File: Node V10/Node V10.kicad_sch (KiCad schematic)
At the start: 6 parts, among them J1 Soil Sensor - 1, J2 Soil Sensor - 2, J3 Soil Sensor - 3, J4 Soil Sensor - 4, U1 MCU

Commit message: Completed schamtic
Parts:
- added J5: PiicoDev, symbol Connector_Generic:Conn_01x04
- added R1, R2: 10k, symbol Device:R
- added TP1: GND_Test, symbol Connector:TestPoint
- added TP2: Vbatt Test, symbol Connector:TestPoint
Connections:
- net SCL: now also J5.1 (Pin_1)
- net SDA: now also J5.2 (Pin_2)
- net GND: now reaches J1.2 (Pin_2)
- net GND: now also J2.2 (Pin_2), J3.2 (Pin_2), J4.2 (Pin_2), U1.100 (Vin_Batt), U1.8 (GND), U2.1 (OUT-), J5.4 (Pin_4), R2.2, TP1.1
- net +3V3: now reaches J1.3 (Pin_3)
- net +3V3: now also J2.3 (Pin_3), J3.3 (Pin_3), J4.3 (Pin_3), U1.9 (3V3), J5.3 (Pin_3)
- net +BATT: now reaches U2.2 (OUT+)
- net +BATT: now also U1.200 (GND_Batt), R1.1, TP2.1
- net Done: now reaches U2.3 (DNE)
- net Done: now also U1.12 (GP44)
- net Vbatt_sense: now reaches U1.5 (GP6)
- net Vbatt_sense: now also R1.2, R2.1
- no-connect marks 0 -> 5
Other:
- note added: "Sensors"
- company: (none) -> Liam Howell
- title: (none) -> PlantPulse Node
- moved on the sheet: J1, J2, J3, J4, U1B, U2

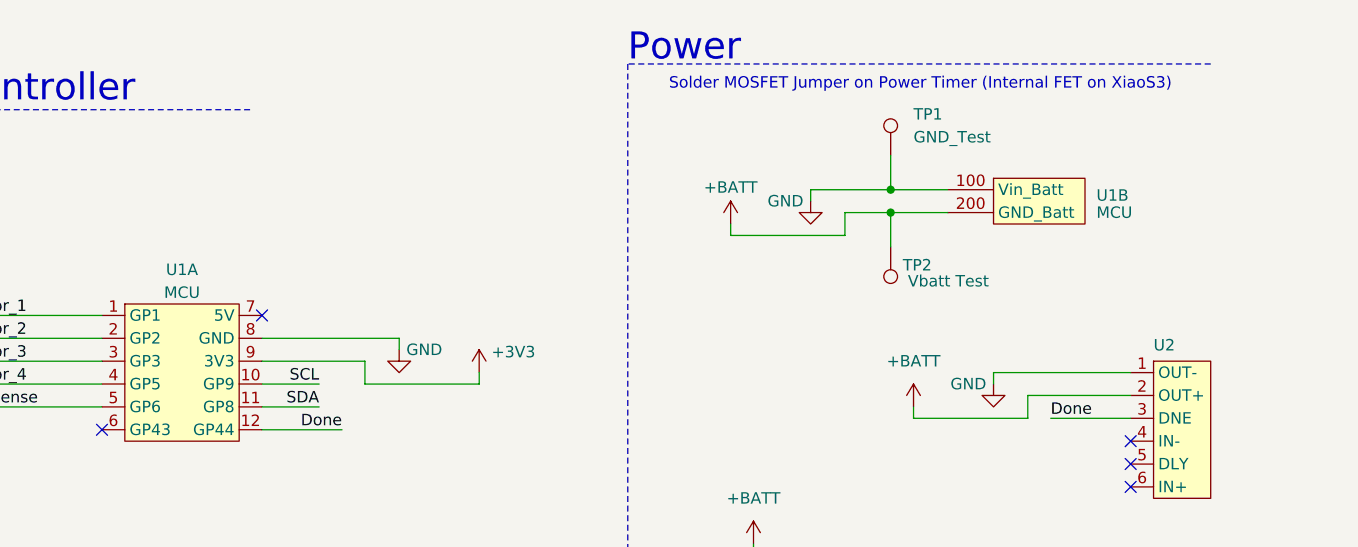
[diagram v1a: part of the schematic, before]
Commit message: Footprints assigned
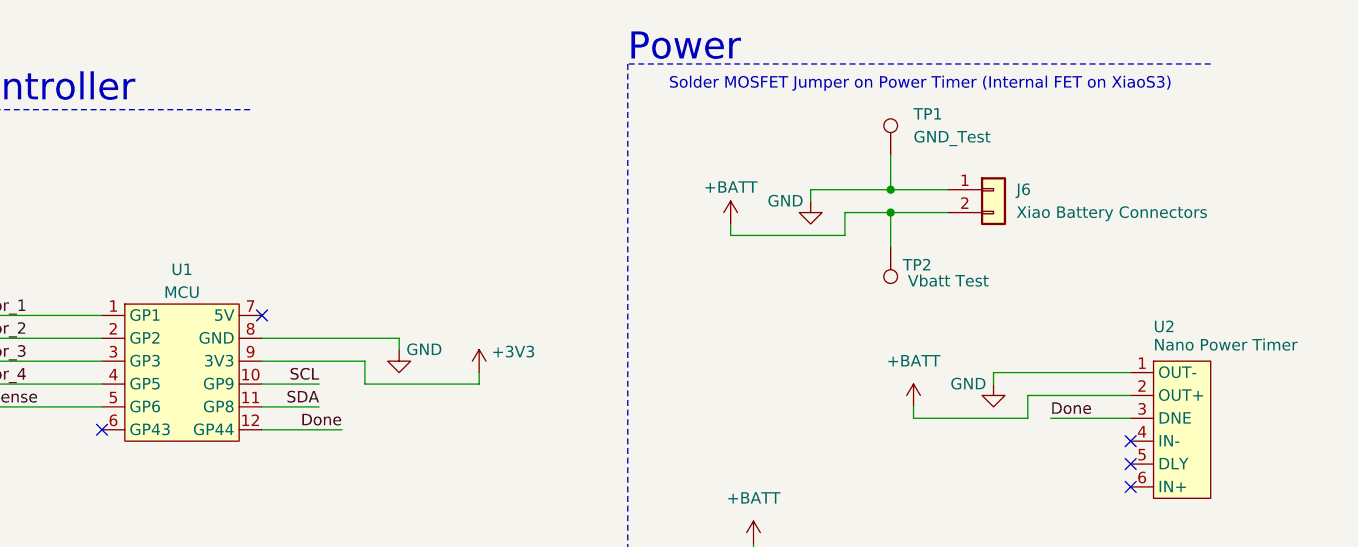
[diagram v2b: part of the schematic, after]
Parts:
- removed unit 2 of U1
- added J6: Xiao Battery Connectors, Connector_PinHeader_2.54mm:PinHeader_1x02_P2.54mm_Horizontal, symbol Connector_Generic:Conn_01x02
- J1, J2, J3, J4: footprint (none) -> Connector_PinHeader_2.54mm:PinHeader_1x03_P2.54mm_Vertical
- J5: footprint (none) -> Footprints-General:PiicoDev Breadboard
- R1, R2: footprint (none) -> Resistor_THT:R_Axial_DIN0207_L6.3mm_D2.5mm_P7.62mm_Horizontal
- TP1, TP2: footprint (none) -> TestPoint:TestPoint_THTPad_1.0x1.0mm_Drill0.5mm
- U1: footprint (none) -> Footprints-General:Xiao-S3
- U2: value ~ -> Nano Power Timer; footprint (none) -> Footprints-General:Nano Power Timer
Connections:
- net +BATT: now also J6.2 (Pin_2)
- net GND: now also J6.1 (Pin_1)
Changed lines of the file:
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@@
 			)
 		)
-		(property "Footprint" ""
+		(property "Footprint" "Connector_PinHeader_2.54mm:PinHeader_1x03_P2.54mm_Vertical"
 			(at 44.45 81.28 0)
 			(effects
@@
 					(reference "#PWR016")
 					(unit 1)
-				)
-			)
-		)
-	)
-	(symbol
-		(lib_id "Liam_Generic_symbols:Xiao_X3_w/_Batt")
-		(at 234.95 78.74 0)
-		(unit 2)
-		(exclude_from_sim no)
-		(in_bom yes)
-		(on_board yes)
-		(dnp no)
-		(fields_autoplaced yes)
-		(property "Reference" "U1"
-			(at 246.38 80.6449 0)
-			(effects
-				(font
-					(size 1.27 1.27)
-				)
-				(justify left)
-			)
-		)
-		(property "Value" "MCU"
-			(at 246.38 82.55 0)
-			(effects
-				(font
-					(size 1.27 1.27)
-				)
-				(justify left)
-			)
-		)
-		(property "Footprint" ""
-			(at 234.95 78.74 0)
-			(effects
-				(font
-					(size 1.27 1.27)
-				)
-				(hide yes)
-			)
-		)
-		(property "Datasheet" ""
-			(at 234.95 78.74 0)
-			(effects
-				(font
-					(size 1.27 1.27)
-				)
-				(hide yes)
-			)
-		)
-		(property "Description" ""
-			(at 234.95 78.74 0)
-			(effects
-				(font
-					(size 1.27 1.27)
-				)
-				(hide yes)
-			)
-		)
-		(pin "5"
-		)
-		(pin "9"
-		)
-		(pin "8"
-		)
-		(pin "3"
-		)
-		(pin "1"
-		)
-		(pin "11"
-		)
-		(pin "200"
-		)
-		(pin "4"
-		)
-		(pin "2"
-		)
-		(pin "6"
-		)
-		(pin "12"
-		)
-		(pin "7"
-		)
-		(pin "10"
-		)
-		(pin "100"
-		)
-		(instances
-			(project "Node V10"
-				(path "/0ed9a77b-3978-4640-876c-ab8d77b25719"
-					(reference "U1")
-					(unit 2)
 				)
 			)
@@
 			)
 		)
-		(property "Footprint" ""
+		(property "Footprint" "Connector_PinHeader_2.54mm:PinHeader_1x03_P2.54mm_Vertical"
 			(at 44.45 123.19 0)
 			(effects
@@
 				(path "/0ed9a77b-3978-4640-876c-ab8d77b25719"
 					(reference "J4")
+					(unit 1)
+				)
+			)
+		)
+	)
+	(symbol
+		(lib_id "Connector_Generic:Conn_01x02")
+		(at 234.95 80.01 0)
+		(unit 1)
+		(exclude_from_sim no)
+		(in_bom yes)
+		(on_board yes)
+		(dnp no)
+		(fields_autoplaced yes)
+		(property "Reference" "J6"
+			(at 237.49 80.0099 0)
+			(effects
+				(font
+					(size 1.27 1.27)
+				)
+				(justify left)
+			)
+		)
+		(property "Value" "Xiao Battery Connectors"
+			(at 237.49 82.5499 0)
+			(effects
+				(font
+					(size 1.27 1.27)
+				)
+				(justify left)
+			)
+		)
+		(property "Footprint" "Connector_PinHeader_2.54mm:PinHeader_1x02_P2.54mm_Horizontal"
+			(at 234.95 80.01 0)
+			(effects
+				(font
+					(size 1.27 1.27)
+				)
+				(hide yes)
+			)
+		)
+		(property "Datasheet" "~"
+			(at 234.95 80.01 0)
+			(effects
+				(font
+					(size 1.27 1.27)
+				)
+				(hide yes)
+			)
+		)
+		(property "Description" "Generic connector, single row, 01x02, script generated (kicad-library-utils/schlib/autogen/connector/)"
+			(at 234.95 80.01 0)
+			(effects
+				(font
+					(size 1.27 1.27)
+				)
+				(hide yes)
+			)
+		)
+		(pin "1"
+		)
+		(pin "2"
+		)
+		(instances
+			(project "Node V10"
+				(path "/0ed9a77b-3978-4640-876c-ab8d77b25719"
+					(reference "J6")
 					(unit 1)
 				)
@@
 			)
 		)
-		(property "Footprint" ""
+		(property "Footprint" "TestPoint:TestPoint_THTPad_1.0x1.0mm_Drill0.5mm"
 			(at 228.6 76.2 0)
 			(effects
@@
 			)
 		)
-		(property "Footprint" ""
+		(property "Footprint" "Resistor_THT:R_Axial_DIN0207_L6.3mm_D2.5mm_P7.62mm_Horizontal"
 			(at 206.502 137.16 90)
 			(effects
@@
 		(dnp no)
 		(property "Reference" "U2"
+			(at 252.73 95.25 0)
+			(effects
+				(font
+					(size 1.27 1.27)
+				)
+				(justify left)
+			)
+		)
+		(property "Value" "Nano Power Timer"
 			(at 252.73 97.282 0)
 			(effects
@@
 			)
 		)
-		(property "Value" "~"
-			(at 260.35 107.95 0)
-			(effects
-				(font
-					(size 1.27 1.27)
-				)
-				(justify left)
-			)
-		)
-		(property "Footprint" ""
+		(property "Footprint" "Footprints-General:Nano Power Timer"
 			(at 252.73 99.06 0)
 			(effects
@@
 			)
 		)
-		(property "Footprint" ""
+		(property "Footprint" "TestPoint:TestPoint_THTPad_1.0x1.0mm_Drill0.5mm"
 			(at 228.6 86.36 0)
 			(effects
@@
 			)
 		)
-		(property "Footprint" ""
+		(property "Footprint" "Connector_PinHeader_2.54mm:PinHeader_1x03_P2.54mm_Vertical"
 			(at 44.45 110.49 0)
 			(effects
@@
 			)
 		)
-		(property "Footprint" ""
+		(property "Footprint" "Resistor_THT:R_Axial_DIN0207_L6.3mm_D2.5mm_P7.62mm_Horizontal"
 			(at 206.502 124.46 90)
 			(effects
@@
 			)
 		)
-		(property "Footprint" ""
+		(property "Footprint" "Footprints-General:PiicoDev Breadboard"
 			(at 44.45 146.05 0)
 			(effects
@@
 			)
 		)
-		(property "Footprint" ""
+		(property "Footprint" "Footprints-General:Xiao-S3"
 			(at 138.43 92.71 0)
 			(effects
@@
 		(pin "4"
 		)
-		(pin "100"
-		)
 		(pin "6"
 		)
@@
 		)
 		(pin "10"
-		)
-		(pin "200"
 		)
 		(instances
@@
 			)
 		)
-		(property "Footprint" ""
+		(property "Footprint" "Connector_PinHeader_2.54mm:PinHeader_1x03_P2.54mm_Vertical"
 			(at 44.45 96.52 0)
 			(effects

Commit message: There are 14 pins oops
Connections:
- net +3V3: now also U1.10 (3V3); no longer U1.9 (3V3)
- net Done: now also U1.13 (GP7); no longer U1.12 (GP44)
- net GND: now also U1.9 (GND); no longer U1.8 (GND)
- net SCL: now also U1.11 (GP9); no longer U1.10 (GP9)
- net SDA: now also U1.12 (GP8); no longer U1.11 (GP8)
- no-connect marks 5 -> 7
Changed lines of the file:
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@@
+	)
+	(no_connect
+		(at 135.89 109.22)
+	)
+	(no_connect
+		(at 153.67 93.98)
+	)
+	(no_connect
+		(at 250.19 107.95)
+	)
+	(no_connect
+		(at 250.19 110.49)
+	)
+	(no_connect
+		(at 153.67 109.22)
 	)
 	(no_connect
 		(at 135.89 106.68)
-	)
-	(no_connect
-		(at 153.67 93.98)
-	)
-	(no_connect
-		(at 250.19 107.95)
-	)
-	(no_connect
-		(at 250.19 110.49)
 	)
 	(wire
@@
 		(pin "10"
 		)
+		(pin "13"
+		)
+		(pin "14"
+		)
 		(instances
